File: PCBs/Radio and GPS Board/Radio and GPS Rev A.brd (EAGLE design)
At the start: 95.9 x 90.2 mm, 7 parts

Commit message: So. many. changes.
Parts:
- removed U$3: PC104_BOARD, PC104 Board:PC104_WITH_CSK_HEADER
- added PINAV_CONNECTOR: HLE-110-02-X-DV-BE-A, HLE-110-02-X-DV-BE-A:HLE-110-02-X-DV-BE-A
- added U$1: PC104_NO_DIMENSION, Cubesat:PC104_NO_DIMENSION
- LITHIUM: value CUBESAT_LITHIUM -> LI-1; device Radio Board Rev B:CUBESAT_LI-1 -> Cubesat:LI-1
- PINAV: value PINAVL1 -> (none); device pinavl1:PINAV-L1 -> Cubesat:PINAV-L1
- moved C3 75.9 mm to (60.6, 6.73)
- moved C4 75.9 mm to (60.6, 4.19)
- moved PINAV 40.3 mm to (80.0, 83.8), turned to 180 degrees
- moved LITHIUM 2.54 mm to (6.35, 11.4)
- moved C1 2.54 mm to (42.5, 29.1)
- moved C2 2.54 mm to (42.7, 60.1)
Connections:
- net 3V3: now also U$1.79; no longer U$3.79
- net GND: now also LITHIUM.THERM1, LITHIUM.THERM2, LITHIUM.THERM3, LITHIUM.THERM4, PINAV_CONNECTOR.15, PINAV_CONNECTOR.7, U$1.100, U$1.61, U$1.66, U$1.69, U$1.73, U$1.74, U$1.81, U$1.82, U$1.84, U$1.99; no longer PINAV.15, PINAV.16, PINAV.3, PINAV.7, U$3.100, U$3.61, U$3.66, U$3.69, U$3.73, U$3.74, U$3.81, U$3.82, U$3.84, U$3.99
- net GPS_PF: now also PINAV_CONNECTOR.6, U$1.24; no longer PINAV.6, U$3.24
- net GPS_RX: now also PINAV_CONNECTOR.2, U$1.35; no longer PINAV.2, U$3.35
- net GPS_TX: now also PINAV_CONNECTOR.1, U$1.33; no longer PINAV.1, U$3.33
- net GPS_VPP: now also PINAV_CONNECTOR.5, U$1.23; no longer PINAV.5, U$3.23
- net LI_RX: now also U$1.29; no longer U$3.29
- net LI_TX: now also U$1.31; no longer U$3.31
- net OA_RESET: now also U$1.47; no longer U$3.47
- net SW3: now also U$1.63; no longer U$3.63
- net SW9: now also PINAV_CONNECTOR.14, PINAV_CONNECTOR.8, U$1.71; no longer PINAV.14, PINAV.8, U$3.71
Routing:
- net GPS_PF: track 56.7 -> 103.9 mm
- net GPS_TX: track 65.0 -> 39.4 mm
- net GPS_RX: track 72.4 -> 56.1 mm
- net GPS_VPP: track 47.7 -> 60.8 mm
- net OA_RESET: track 82.2 -> 95.2 mm
- net SW3: track 67.0 -> 63.1 mm
- net 3V3: track 58.1 -> 55.6 mm
- net SW9: track 102.0 -> 104.3 mm
- net GND: track 29.5 -> 27.4 mm, vias 16 -> 10
- net LI_RX: track 56.0 -> 55.3 mm
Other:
- outline, holes or cut-outs redrawn

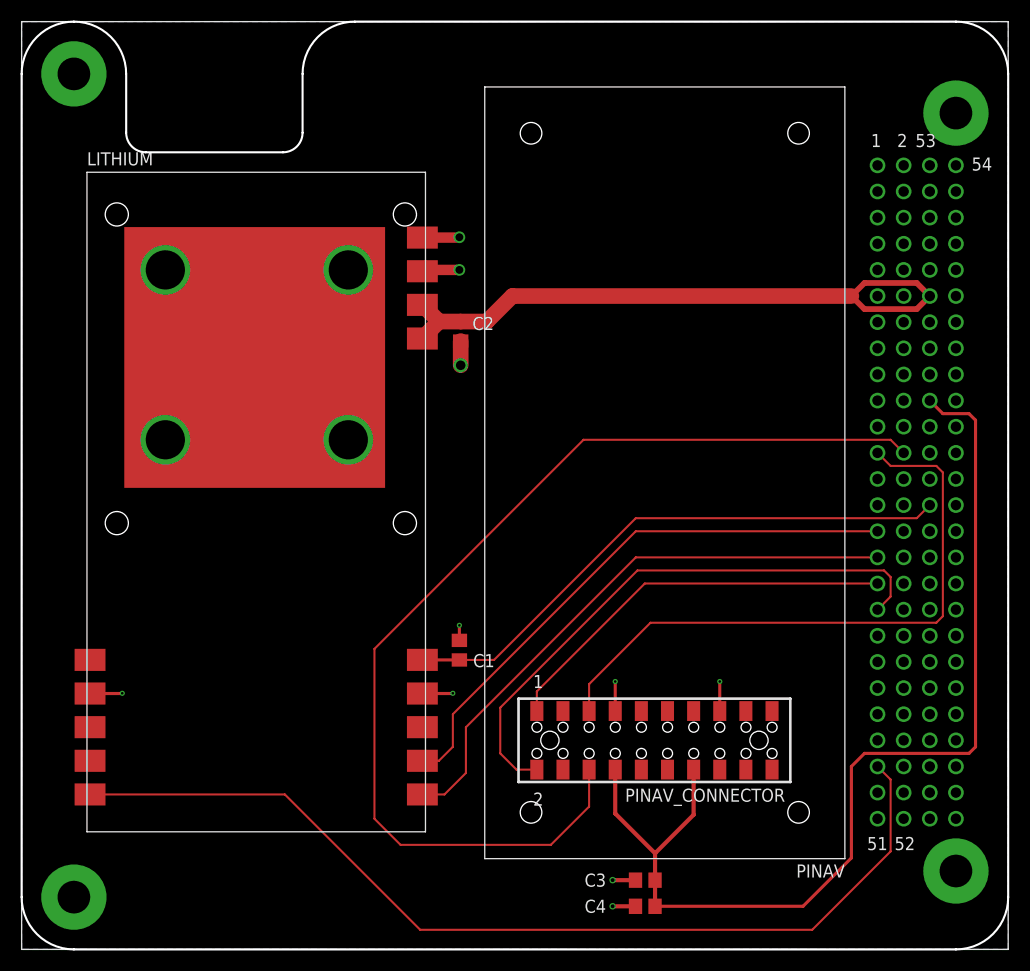
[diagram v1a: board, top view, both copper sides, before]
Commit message: Add testpads, improve bypassing, update routing
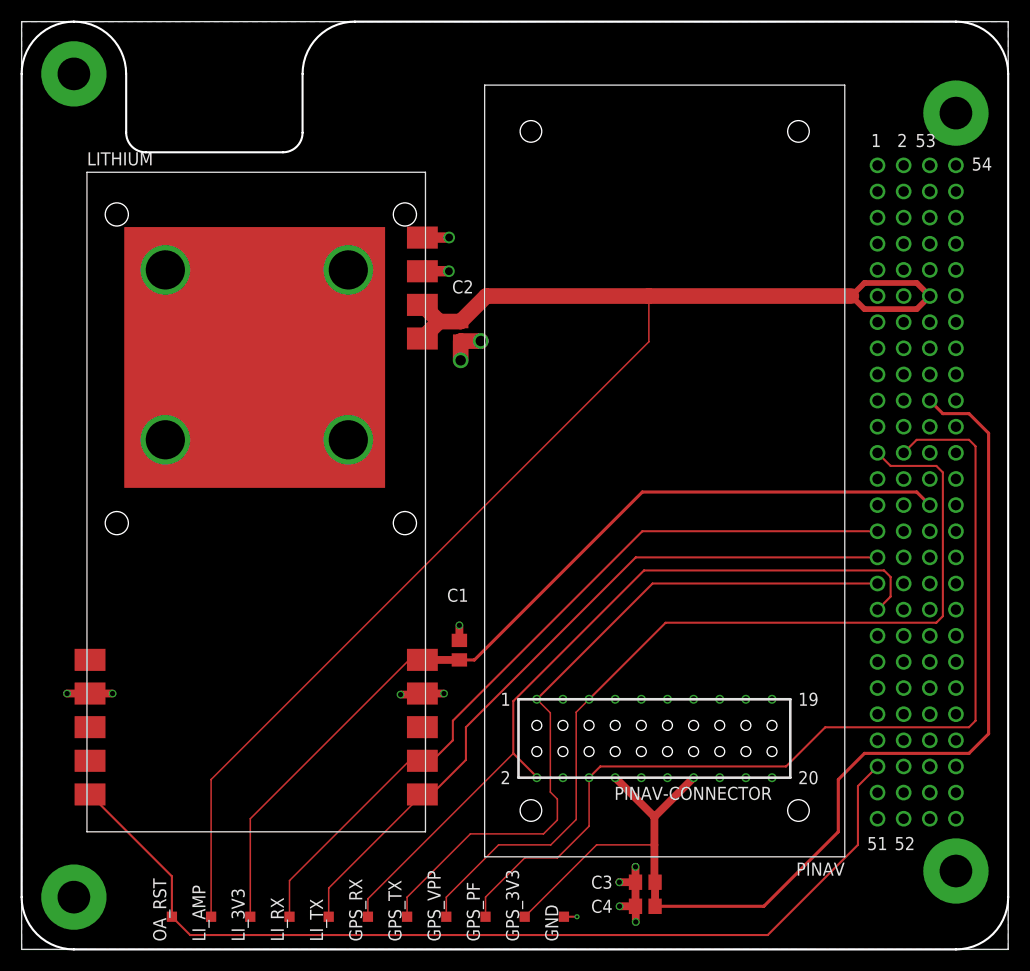
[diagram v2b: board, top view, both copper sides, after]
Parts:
- removed PINAV_CONNECTOR: HLE-110-02-X-DV-BE-A, HLE-110-02-X-DV-BE-A:HLE-110-02-X-DV-BE-A
- added GND, GPS_3V3, GPS_PF, GPS_RX, GPS_TX, GPS_VPP, LI_3V3, LI_AMP, LI_RX, LI_TX, OA_RST: TPSQTP10SQ, testpad:TP10SQ
- added PINAV-CONNECTOR: HLE-110-02-X-DVHLE-110-X-DV-PE-BA, HLE-110-02-X-DV:HLE-110-02-X-DV-PE-BE
- C2: value 10uF -> 47uF
- C3: value 1uF -> 0.1uF
- C4: value 0.1uF -> 1uF
- moved C3 0.20 mm to (60.6, 6.53)
- moved PINAV 0.18 mm to (80.0, 84.0)
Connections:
- net 3V3: now also LI_3V3.TP
- net GND: now also GND.TP, PINAV-CONNECTOR.P$15, PINAV-CONNECTOR.P$7; no longer PINAV_CONNECTOR.15, PINAV_CONNECTOR.7
- net GPS_PF: now also GPS_PF.TP, PINAV-CONNECTOR.P$6; no longer PINAV_CONNECTOR.6
- net GPS_RX: now also GPS_RX.TP, PINAV-CONNECTOR.P$2; no longer PINAV_CONNECTOR.2
- net GPS_TX: now also GPS_TX.TP, PINAV-CONNECTOR.P$1; no longer PINAV_CONNECTOR.1
- net GPS_VPP: now also GPS_VPP.TP, PINAV-CONNECTOR.P$5; no longer PINAV_CONNECTOR.5
- net LI_RX: now also LI_RX.TP
- net LI_TX: now also LI_TX.TP
- net OA_RESET: now also OA_RST.TP
- net SW3: now also LI_AMP.TP
- net SW9: now also GPS_3V3.TP, PINAV-CONNECTOR.P$14, PINAV-CONNECTOR.P$8; no longer PINAV_CONNECTOR.14, PINAV_CONNECTOR.8
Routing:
- net SW3: track 63.1 -> 141.0 mm
- net 3V3: track 55.6 -> 89.2 mm
- net GPS_TX: track 39.4 -> 70.0 mm
- net GPS_VPP: track 60.8 -> 88.7 mm
- net LI_RX: track 55.3 -> 75.8 mm
- net GPS_RX: track 56.1 -> 76.0 mm
- net LI_TX: track 56.4 -> 71.3 mm
- net GPS_PF: track 103.9 -> 93.8 mm
- net SW9: track 104.3 -> 113.6 mm
- net GND: track 27.4 -> 28.9 mm, vias 10 -> 14

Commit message: Replace radio with Li-2 footprint
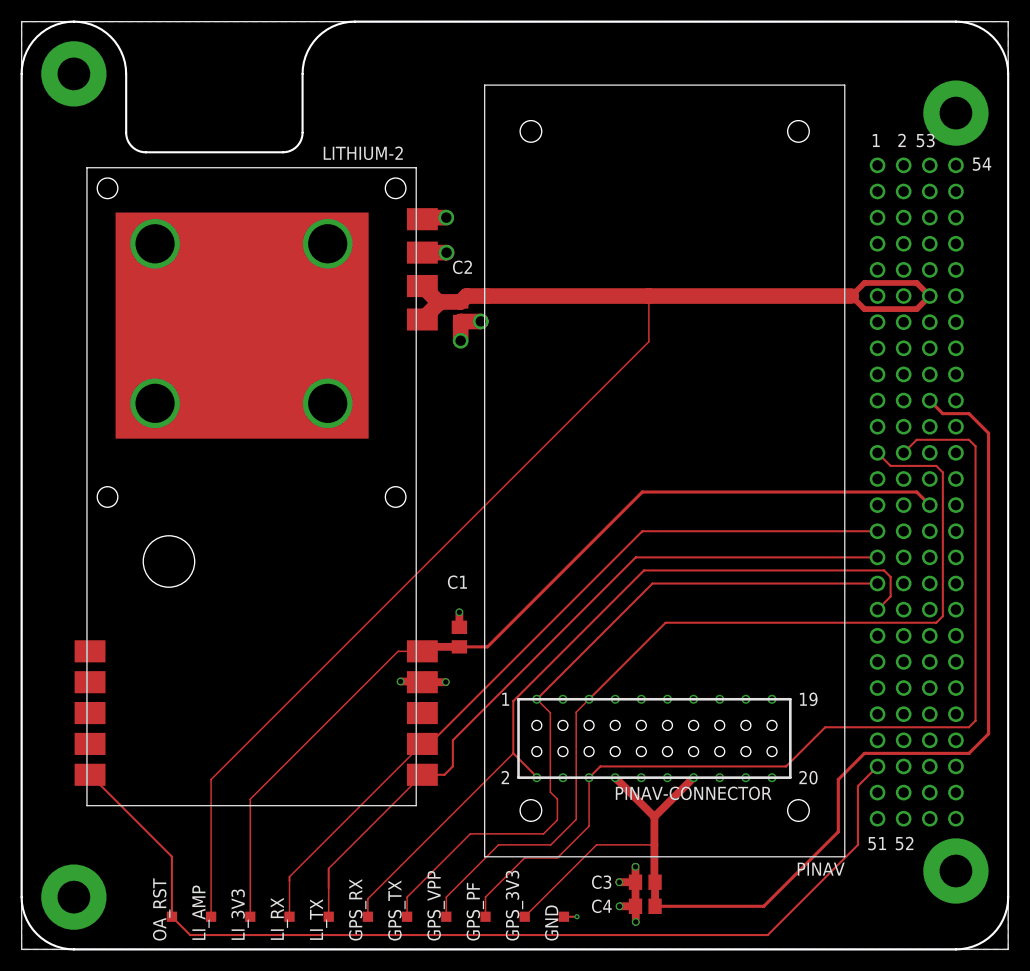
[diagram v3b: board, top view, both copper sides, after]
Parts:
- removed LITHIUM: LI-1, Cubesat:LI-1
- added LITHIUM-2: LI-2, Cubesat:LI-2
- moved C2 1.91 mm to (42.7, 62.0)
- moved C1 1.27 mm to (42.5, 30.4)
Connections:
- net 3V3: now also LITHIUM-2.3.3V; no longer LITHIUM.3.3V
- net GND: now also LITHIUM-2.GND2, LITHIUM-2.RF_GND, LITHIUM-2.RF_GND1, LITHIUM-2.RF_GND2, LITHIUM-2.THERM1, LITHIUM-2.THERM2, LITHIUM-2.THERM3, LITHIUM-2.THERM4; no longer LITHIUM.GND1, LITHIUM.GND2, LITHIUM.RF_GND1, LITHIUM.RF_GND2, LITHIUM.RF_GND3, LITHIUM.THERM1, LITHIUM.THERM2, LITHIUM.THERM3, LITHIUM.THERM4
- net LI_RX: now also LITHIUM-2.RX_UART; no longer LITHIUM.RX_UART
- net LI_TX: now also LITHIUM-2.TX_UART; no longer LITHIUM.TX_UART
- net OA_RESET: now also LITHIUM-2.CONFIG1; no longer LITHIUM.CONFIG1
- net SW3: now also LITHIUM-2.V_AMP1, LITHIUM-2.V_AMP2; no longer LITHIUM.V_AMP1, LITHIUM.V_AMP2
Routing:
- net GND: track 28.9 -> 24.2 mm, vias 14 -> 12
- net OA_RESET: track 94.9 -> 96.5 mm
- net 3V3: track 89.2 -> 90.4 mm
- net LI_RX: track 75.8 -> 74.9 mm
- net LI_TX: track 71.3 -> 72.0 mm
- net SW3: track 141.0 -> 140.5 mm

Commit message: Add rev info to silkscreen
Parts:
- moved C1 2.92 mm to (42.5, 27.4), turned to 270 degrees
- moved C2 2.43 mm to (42.4, 64.4), turned to 90 degrees
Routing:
- net 3V3: track 90.4 -> 91.5 mm
- net GND: track 24.2 -> 24.5 mm, vias 12 -> 8
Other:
- board text added: "VT VCC Communications Board Rev A - 7/31/18"
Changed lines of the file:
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@@
 <layer number="27" name="tValues" color="7" fill="1" visible="yes" active="yes"/>
 <layer number="28" name="bValues" color="7" fill="1" visible="no" active="yes"/>
-<layer number="29" name="tStop" color="7" fill="3" visible="no" active="yes"/>
+<layer number="29" name="tStop" color="7" fill="3" visible="yes" active="yes"/>
 <layer number="30" name="bStop" color="7" fill="6" visible="no" active="yes"/>
 <layer number="31" name="tCream" color="7" fill="4" visible="no" active="yes"/>
@@
 <layer number="46" name="Milling" color="3" fill="1" visible="no" active="yes"/>
 <layer number="47" name="Measures" color="7" fill="1" visible="no" active="yes"/>
-<layer number="48" name="Document" color="7" fill="1" visible="no" active="yes"/>
+<layer number="48" name="Document" color="7" fill="1" visible="yes" active="yes"/>
 <layer number="49" name="Reference" color="7" fill="1" visible="no" active="yes"/>
 <layer number="50" name="dxf" color="7" fill="1" visible="no" active="no"/>
@@
 <wire x1="27.305" y1="85.09" x2="32.385" y2="90.17" width="0.2032" layer="20" curve="-90"/>
 <wire x1="32.385" y1="90.17" x2="90.805" y2="90.17" width="0.2032" layer="20"/>
+<text x="69.215" y="88.9" size="1.778" layer="48" rot="R180">VT VCC Communications Board
+Rev A - 7/31/18</text>
 </plain>
 <attributes>
@@
 </autorouter>
 <elements>
-<element name="C1" library="resistor" library_urn="urn:adsk.eagle:library:348" package="C0805" package3d_urn="urn:adsk.eagle:package:23617/2" value="0.1uF" x="42.545" y="30.353" smashed="yes" rot="R90">
-<attribute name="NAME" x="43.434" y="36.322" size="1.27" layer="25" rot="R180"/>
-<attribute name="VALUE" x="44.577" y="34.544" size="1.27" layer="27" rot="R180"/>
-</element>
-<element name="C2" library="resistor" library_urn="urn:adsk.eagle:library:348" package="C0805" package3d_urn="urn:adsk.eagle:package:23617/2" value="47uF" x="42.672" y="61.976" smashed="yes" rot="R270">
-<attribute name="NAME" x="41.8338" y="65.659" size="1.27" layer="25"/>
-<attribute name="VALUE" x="40.767" y="64.135" size="1.27" layer="27"/>
+<element name="C1" library="resistor" library_urn="urn:adsk.eagle:library:348" package="C0805" package3d_urn="urn:adsk.eagle:package:23617/2" value="0.1uF" x="42.545" y="27.432" smashed="yes" rot="R270">
+<attribute name="NAME" x="41.656" y="21.463" size="1.27" layer="25"/>
+<attribute name="VALUE" x="40.513" y="23.241" size="1.27" layer="27"/>
+</element>
+<element name="C2" library="resistor" library_urn="urn:adsk.eagle:library:348" package="C0805" package3d_urn="urn:adsk.eagle:package:23617/2" value="47uF" x="42.418" y="64.389" smashed="yes" rot="R90">
+<attribute name="NAME" x="43.2562" y="60.706" size="1.27" layer="25" rot="R180"/>
+<attribute name="VALUE" x="44.323" y="62.23" size="1.27" layer="27" rot="R180"/>
 </element>
 <element name="C3" library="resistor" library_urn="urn:adsk.eagle:library:348" package="C0805" package3d_urn="urn:adsk.eagle:package:23617/2" value="0.1uF" x="60.613" y="6.531" smashed="yes" rot="R180">
@@
 <attribute name="VALUE" x="65.947" y="4.826" size="1.27" layer="27" rot="R180"/>
 </element>
-<element name="PINAV" library="Cubesat" package="PINAV-L1" value="" x="80" y="84" rot="R180"/>
+<element name="PINAV" library="Cubesat" package="PINAV-L1" value="" x="80" y="84" smashed="yes" rot="R180">
+<attribute name="NAME" x="74.3558" y="84.5798" size="1.27" layer="25"/>
+</element>
 <element name="U$1" library="Cubesat" package="PC104_NO_DIMENSION" value="PC104_NO_DIMENSION" x="0" y="0"/>
 <element name="PINAV-CONNECTOR" library="HLE-110-02-X-DV" package="HLE-110-02-X-DV-PE-BE" value="HLE-110-02-X-DVHLE-110-X-DV-PE-BA" x="61.5" y="20.5" rot="R180"/>
@@
 <wire x1="39.149" y1="61.021" x2="38.95" y2="61.22" width="1.524" layer="1"/>
 <wire x1="45.151" y1="63.5" x2="45.151" y2="63.5" width="1.524" layer="1"/>
-<wire x1="45.151" y1="63.5" x2="43.246" y2="63.5" width="1.524" layer="1"/>
-<wire x1="43.246" y1="63.5" x2="42.672" y2="62.926" width="1.524" layer="1"/>
-<wire x1="42.672" y1="62.926" x2="40.494" y2="62.926" width="1.524" layer="1"/>
 <wire x1="40.494" y1="62.926" x2="38.95" y2="64.47" width="1.524" layer="1"/>
 <wire x1="38.95" y1="61.22" x2="40.494" y2="62.764" width="1.524" layer="1"/>
 <wire x1="40.494" y1="62.764" x2="40.494" y2="62.926" width="1.524" layer="1"/>
+<wire x1="42.418" y1="63.439" x2="41.743" y2="62.764" width="1.524" layer="1"/>
+<wire x1="41.743" y1="62.764" x2="40.494" y2="62.764" width="1.524" layer="1"/>
+<wire x1="42.418" y1="63.439" x2="42.479" y2="63.5" width="1.524" layer="1"/>
+<wire x1="42.479" y1="63.5" x2="45.151" y2="63.5" width="1.524" layer="1"/>
 </signal>
 <signal name="OA_RESET">
@@
 <contactref element="C1" pad="2"/>
 <contactref element="C2" pad="2"/>
-<via x="42.545" y="32.766" extent="1-16" drill="0.508"/>
-<wire x1="42.672" y1="61.026" x2="42.672" y2="59.1566" width="1.524" layer="1"/>
-<via x="42.672" y="59.1566" extent="1-16" drill="1.016"/>
 <polygon width="0.2032" layer="16">
 <vertex x="0" y="90.17"/>
@@
 <vertex x="0" y="0"/>
 </polygon>
-<wire x1="42.545" y1="31.303" x2="42.545" y2="32.766" width="0.762" layer="1"/>
 <contactref element="C4" pad="2"/>
 <contactref element="C3" pad="2"/>
@@
 <wire x1="59.69" y1="4.164" x2="59.69" y2="2.667" width="0.762" layer="1"/>
 <via x="59.69" y="2.667" extent="1-16" drill="0.508"/>
-<wire x1="42.672" y1="61.026" x2="44.6176" y2="61.026" width="1.524" layer="1"/>
-<wire x1="44.6278" y1="61.0362" x2="44.6176" y2="61.026" width="1.524" layer="1"/>
-<via x="44.6278" y="61.0362" extent="1-16" drill="1.016"/>
 <contactref element="GND" pad="TP"/>
 <wire x1="52.705" y1="3.175" x2="53.975" y2="3.175" width="0.2032" layer="1"/>
@@
 <contactref element="LITHIUM-2" pad="RF_GND"/>
 <wire x1="38.95" y1="70.97" x2="39.1" y2="71.12" width="1.524" layer="1"/>
-<wire x1="39.1" y1="71.12" x2="41.275" y2="71.12" width="1.524" layer="1"/>
-<via x="41.275" y="71.12" extent="1-16" drill="1.016"/>
-<wire x1="38.95" y1="67.72" x2="41.2968" y2="67.72" width="1.524" layer="1"/>
-<wire x1="41.2968" y1="67.72" x2="41.3004" y2="67.7164" width="1.524" layer="1"/>
-<via x="41.3004" y="67.7164" extent="1-16" drill="1.016"/>
-<wire x1="38.95" y1="25.97" x2="41.21" y2="25.97" width="0.762" layer="1"/>
-<wire x1="41.21" y1="25.97" x2="41.2242" y2="25.9842" width="0.762" layer="1"/>
-<via x="41.2242" y="25.9842" extent="1-16" drill="0.508"/>
+<wire x1="39.1" y1="71.12" x2="41.91" y2="71.12" width="1.524" layer="1"/>
+<via x="41.91" y="71.12" extent="1-16" drill="1.016"/>
 <wire x1="38.95" y1="25.97" x2="38.885" y2="26.035" width="0.762" layer="1"/>
-<wire x1="38.885" y1="26.035" x2="36.83" y2="26.035" width="0.762" layer="1"/>
-<via x="36.83" y="26.035" extent="1-16" drill="0.508"/>
+<wire x1="42.418" y1="65.339" x2="40.037" y2="67.72" width="1.524" layer="1"/>
+<wire x1="40.037" y1="67.72" x2="38.95" y2="67.72" width="1.524" layer="1"/>
+<wire x1="42.418" y1="65.339" x2="42.484" y2="65.405" width="1.524" layer="1"/>
+<wire x1="42.484" y1="65.405" x2="44.45" y2="65.405" width="1.524" layer="1"/>
+<via x="44.45" y="65.405" extent="1-16" drill="1.016"/>
+<wire x1="42.545" y1="26.482" x2="39.462" y2="26.482" width="0.762" layer="1"/>
+<wire x1="39.462" y1="26.482" x2="38.95" y2="25.97" width="0.762" layer="1"/>
+<wire x1="42.545" y1="26.482" x2="42.545" y2="25.1714" width="0.762" layer="1"/>
+<via x="42.545" y="25.1714" extent="1-16" drill="0.508"/>
 <wire x1="29.75" y1="53.07" x2="21.43" y2="60.63" width="0" layer="19" extent="1-1"/>
 </signal>
@@
 <signal name="3V3">
 <contactref element="C1" pad="1"/>
-<wire x1="60.325" y1="44.45" x2="86.995" y2="44.45" width="0.3048" layer="1"/>
-<wire x1="60.325" y1="44.45" x2="45.278" y2="29.403" width="0.3048" layer="1"/>
-<wire x1="45.278" y1="29.403" x2="42.545" y2="29.403" width="0.3048" layer="1"/>
+<wire x1="86.995" y1="44.45" x2="60.325" y2="44.45" width="0.3048" layer="1"/>
 <contactref element="U$1" pad="79"/>
 <contactref element="LI_3V3" pad="TP"/>
 <wire x1="86.995" y1="44.45" x2="88.265" y2="43.18" width="0.3048" layer="1"/>
 <contactref element="LITHIUM-2" pad="3.3V"/>
-<wire x1="42.545" y1="29.403" x2="39.383" y2="29.403" width="0.762" layer="1"/>
 <wire x1="39.383" y1="29.403" x2="38.95" y2="28.97" width="0.762" layer="1"/>
 <wire x1="38.95" y1="28.97" x2="36.59" y2="28.97" width="0.1524" layer="1"/>
 <wire x1="36.59" y1="28.97" x2="22.225" y2="14.605" width="0.1524" layer="1"/>
 <wire x1="22.225" y1="14.605" x2="22.225" y2="3.175" width="0.1524" layer="1"/>
+<wire x1="42.545" y1="28.382" x2="39.538" y2="28.382" width="0.762" layer="1"/>
+<wire x1="44.257" y1="28.382" x2="42.545" y2="28.382" width="0.3048" layer="1"/>
+<wire x1="60.325" y1="44.45" x2="44.257" y2="28.382" width="0.3048" layer="1"/>
+<wire x1="39.538" y1="28.382" x2="38.95" y2="28.97" width="0.762" layer="1"/>
 </signal>
 </signals>
@@
 </drawing>
 <compatibility>
+<note version="6.3" minversion="6.2.2" severity="warning">
+Since Version 6.2.2 text objects can contain more than one line,
+which will not be processed correctly with this version.
+</note>
 <note version="8.2" severity="warning">
 Since Version 8.2, EAGLE supports online libraries. The ids
